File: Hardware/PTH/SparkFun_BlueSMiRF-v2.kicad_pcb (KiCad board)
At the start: 2 copper layers, 38.1 x 15.2 mm, 57 parts, among them J1 Conn_01x06, Q1 Q_NMOS_DGS, Q2 Q_NMOS_DGS, SW1 Switch, U1 ESP32_Pico_Mini, U2 AP2112K-3.3

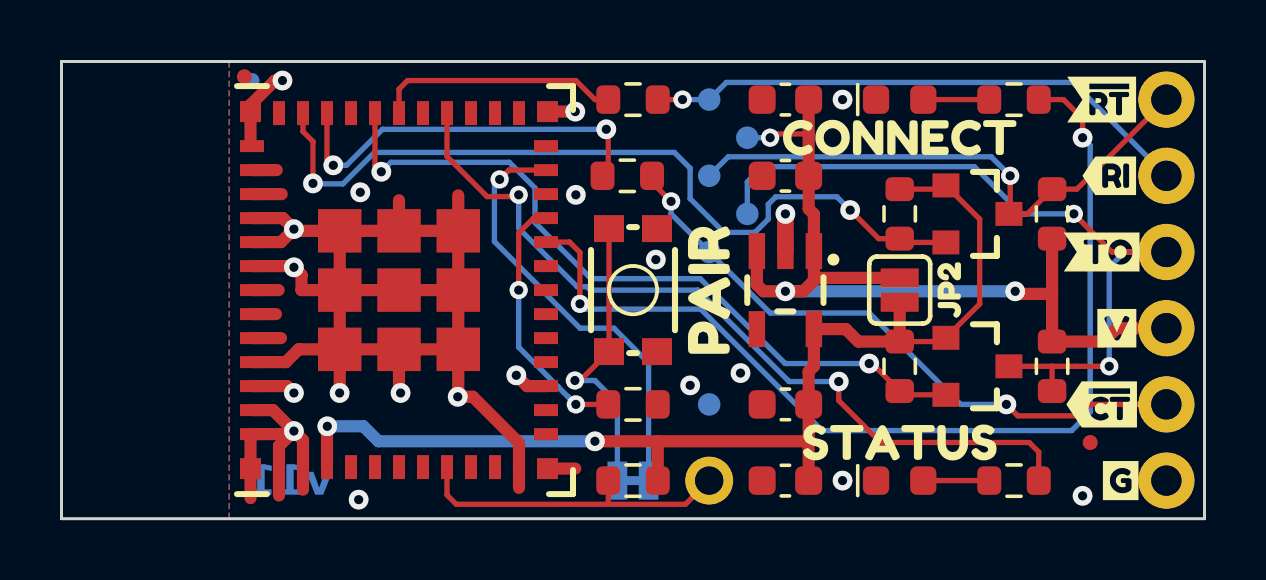
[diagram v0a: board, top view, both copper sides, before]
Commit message: Update 3D models and components to current library
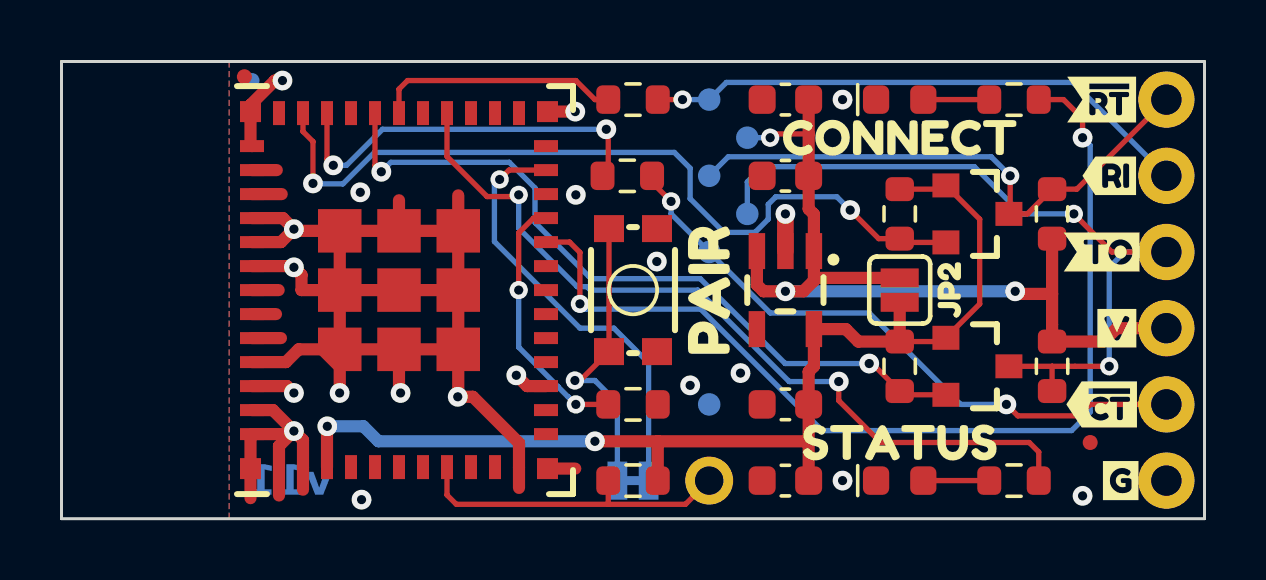
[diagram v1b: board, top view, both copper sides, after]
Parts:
- FID1, FID2, FID3, FID4: value Fiducial_0.5 -> Fiducial_0.5mm
- U1: footprint SparkFun-RF:ESP32-MINI -> SparkFun-RF:ESP32-PICO-MINI

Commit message: Fixing switch
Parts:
- D1: footprint SparkFun-LED:LED_0603_1608Metric -> SparkFun-LED:LED_0603_1608Metric_Green
- D2: footprint SparkFun-LED:LED_0603_1608Metric -> SparkFun-LED:LED_0603_1608Metric_Red
- J1: footprint SparkFun-Connector:1X06 -> SparkFun-Connector:1x06
- JP1: footprint SparkFun-Jumper:SMT-JUMPER_2_NC_TRACE_SILK -> SparkFun-Jumper:Jumper_2_NC_Trace
- JP2: footprint SparkFun-Jumper:SMT-JUMPER_2_NO_SILK -> SparkFun-Jumper:Jumper_2_NO
- Q1, Q2: value Q_NMOS_DGS -> BSS138
- SW1: value Switch -> SMD_4.6x2.8mm_h2.5mm; footprint SparkFun-Switch:Momentary_SMD_4.6x2.8mm -> SparkFun-Switch:Push_SMD_4.6x2.8mm_h2.5mm
- TP1: value TestPoint -> PTH; footprint SparkFun-Connector:1X01 -> SparkFun-Connector:1x01
- TP2, TP3, TP4, TP5, TP6, TP7: value TestPoint_0.75mm -> 0.75mm
- U1: value ESP32_Pico_Mini -> ESP32-PICO-V3-02
- U3: footprint SparkFun-Aesthetic:ORDERING_INSTRUCTIONS -> SparkFun-Aesthetic:Ordering_Instructions
